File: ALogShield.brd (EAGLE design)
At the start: 53.3 x 77.5 mm, 36 parts, among them IC1 LTC4412, J1 POWER_JACKPTH, Q1 FDN360P, Q2 FDN360P

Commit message: Transitioning to 2.0 update
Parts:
- removed CLOCK_BATT: 3V Backup Battery, SparkFun:BATTCON_12MM_PTH
- removed COUT: 1uF, SmartPrj:C0603-ROUND
- removed C_LDO_SD, C_LDO_SENSE: >=2.2uF, resistor:C0603
- removed DECOUP: >=1uF, resistor:C0603
- removed H0: (no value), SparkFun:SCREWTERMINAL-3.5MM-8
- removed IC1: LTC4412, awickert:TSOT23-6
- removed ISP: AVRISP-6, adafruit:AVRISP
- removed LD0_SD, LD0_SENSE: LP2985, adafruit:SOT23-5L
- removed LED: (no value), SparkFun:LED3MM
- removed LOGO1: OSHW-LOGOM, SparkFun-Aesthetics:OSHW-LOGO-M
- removed LSHIFT: 4050D, 40xx:SO16
- removed MANUAL_LOG: Log Now, awickert:TL_BUTTON
- removed PU1, PU2: 4.7K, rcl:R0603
- removed Q1, Q2: FDN360P, transistor-power:SUPER-SOT3
- removed RSTAT: 470k, rcl:R0603
- removed RTC: DS3231SN, comfile:SO16W
- removed R_LED: 330, rcl:R0603
- removed R_REF_A0: Therm, resistor:0207/10
- removed R_REF_A1, R_REF_A2, R_REF_A3, R_REF_A6, R_REF_A7: (no value), resistor:0207/10
- removed S2: Reset, SparkFun:TACTILE_SWITCH_SMD
- removed U$2: ALOG_LOGO_V1_5.5MM, awickert:ALOG_LOGO_V1_SMALL
- removed U$3: NWLOGO_MED, awickert:NWLOGO_MED
- added 3V3: (no value), csandell:6-TMLF
- added A0, A1, A2, A3: (no value), resistor:0207/10
- added C14: 10nF, rc-master-smd:CECJ-1206
- added CLOCK_BATT1: 3V Backup Battery, SparkFun:BATTCON_12MM_PTH
- added CLOCK_BATT_DECOUP, COUT1: 0.1uF, rcl:C0603
- added CLOCK_BATT_DECOUPLE: 10uF, SparkFun-Passives:EIA3216
- added CLOCK_CIN1, CLOCK_CIN2, CLOCK_CIN3: 1uF, rcl:C0603
- added D1: BAT54C, semicon-smd-ipc:SOT23C
- added D2: BAT54, semicon-smd-ipc:SOT23C
- added H4, H5: (no value), SparkFun-Connectors:SCREWTERMINAL-3.5MM-8
- added ISP1: AVRISP-6, adafruit:AVRISP
- added LED1: (no value), SparkFun:LED3MM
- added LOG: LOG, SparkFun-Electromechanical:TACTILE-PTH
- added LOGO2: OSHW-LOGOM, SparkFun-Aesthetics:OSHW-LOGO-M
- added LSHIFT1: 4050D, 40xx:SO16
- added Q3, Q4: 2N7002PW, SparkFun-DiscreteSemi:SOT323
- added RCKL1, RCLK2: 220, rcl:R0603
- added RESET: Reset, SparkFun-Electromechanical:TACTILE-PTH
- added RN2: 3.3K, resistor-dil:0603-ARC
- added R_LED1: 220, resistor:R0603
- added R_RESET: 10k, rcl:R0603
- added U$1: ALOG_LOGO_V1_5.5MM, awickert:ALOG_LOGO_V1_SMALL
- added U$4: NWLOGO, awickert:NWLOGO
- added U$5: NWLOGO_MED, awickert:NWLOGO_MED
- added U1: DS3231MZ/V+T, Maxim-DS3231MZ_8-SOIC:21-0041B_8
- H2: device SparkFun:SCREWTERMINAL-3.5MM-4 -> SparkFun:SCREWTERMINAL-3.5MM-8
- J1: value POWER_JACKPTH -> (none); device SparkFun:POWER_JACK_PTH -> SparkFun-Connectors:SCREWTERMINAL-3.5MM-4
- moved J1 145.8 mm to (-5.08, -111.1), turned to 0 degrees
- moved H2 113.6 mm to (-4.45, -103.5)
- renumbered SD to SD1
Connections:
- removed net A6: H2.1, R_REF_A6.2
- removed net A7: H2.3, R_REF_A7.2
- removed net BATTERY_POWER: IC1.1, Q1.3
- removed net CD_NOT_CONNECTED: SD1.CD
- removed net D4-SENSE_3V3_SWITCH: LD0_SENSE.3, U$9.D4
- removed net D8-SD_3V3_SWITCH: LD0_SD.3, U$9.D8
- removed net LED+: LED.A, R_LED.2
- removed net N$7: IC1.4, Q2.1, RSTAT.1
- removed net N$8: IC1.5, Q1.1
- removed net VUSB: Q2.3
- new net 5V: H5.9
- new net CS-SD: LSHIFT1.7
- new net D4-SENSE_LDO_SWITCH: 3V3.4, U$9.D4
- new net D6-CLOCK_SD_SWITCH: 3V3.3, U$9.D6
- new net D7-CS-EXT: H5.7, U$9.D7
- new net D8-EXT: H5.6, U$9.D8
- new net DTR: COUT1.1
- new net LED+1: LED1.A, R_LED1.2
- new net N$1: D1.1, RCLK2.1
- new net N$11: D2.3, LOG.3
- new net N$2: CLOCK_BATT1.VCC@1, RCLK2.2
- new net N$67: D1.2, RCKL1.1
- new net SCL_3V3: Q4.2, RN2.3, U1.8
- new net SDA_3V3: Q3.2, RN2.4, U1.7
- net +3V3: now also 3V3.1, CLOCK_CIN2.1, H2.6, H2.8, H5.8; no longer C_LDO_SENSE.2, H0.2, H0.4, H0.6, H0.8, LD0_SENSE.5
- net A0: now also A0.2, C14.C1, H2.1; no longer H0.1, R_REF_A0.2
- net A1: now also A1.2, C14.D1, H2.3; no longer H0.3, R_REF_A1.2
- net A2: now also A2.2, C14.A1, H2.5; no longer H0.5, R_REF_A2.2
- net A3: now also A3.2, C14.B1, H2.7; no longer H0.7, R_REF_A3.2
- net BAT: now also CLOCK_BATT_DECOUP.1, CLOCK_BATT_DECOUPLE.A, D1.3, U1.6; no longer CLOCK_BATT.VCC@1, RTC.14
- net CLK: now also H5.4, ISP1.3, LSHIFT1.3; no longer ISP.3, LSHIFT.3
- net CS: no longer LSHIFT.7
- net D3-INT1: now also H4.3
- net D5_MANUAL_LOG: now also D2.2; no longer MANUAL_LOG.1
- net D6: no longer U$9.D6
- net D7: no longer U$9.D7
- net D9-LED: now also R_LED1.1; no longer R_LED.1
- net DI: now also H5.2, ISP1.4, LSHIFT1.5; no longer ISP.4, LSHIFT.5
- net DO: now also H5.3, ISP1.1; no longer ISP.1
- net GND: now also 3V3.5, A0.1, A1.1, A2.1, A3.1, C14.A2, C14.B2, C14.C2, C14.D2, CLOCK_BATT1.GND, CLOCK_BATT_DECOUP.2, CLOCK_BATT_DECOUPLE.C, CLOCK_CIN1.2, CLOCK_CIN2.2, CLOCK_CIN3.2, H4.6, H5.1, H5.10, ISP1.6, J1.2, LED1.K, LOG.1, LSHIFT1.11, LSHIFT1.14, LSHIFT1.8, LSHIFT1.9, RESET.1, U1.5; no longer CLOCK_BATT.GND, COUT.2, C_LDO_SD.1, C_LDO_SENSE.1, DECOUP.2, IC1.2, IC1.3, ISP.6, J1.GND, J1.GNDBREAK, LD0_SD.2, LD0_SENSE.2, LED.K, LSHIFT.11, LSHIFT.14, LSHIFT.8, LSHIFT.9, MANUAL_LOG.C1, MANUAL_LOG.C2, RTC.10, RTC.11, RTC.12, RTC.13, RTC.5, RTC.6, RTC.7, RTC.8, RTC.9, R_REF_A0.1, R_REF_A1.1, R_REF_A2.1, R_REF_A3.1, R_REF_A6.1, R_REF_A7.1, S2.1, S2.2
- net INT0: now also D2.1, U1.3; no longer MANUAL_LOG.2, RTC.3
- net RESET: now also COUT1.2, ISP1.5, RESET.3, R_RESET.1; no longer ISP.5, S2.3, S2.4
- net RX-I: now also H4.7
- net SCL: now also H4.10, Q4.3, RN2.7; no longer PU1.1, RTC.16
- net SDA: now also H4.9, Q3.3, RN2.8; no longer PU2.1, RTC.15
- net SD_CLK: now also LSHIFT1.2; no longer LSHIFT.2
- net SD_CS: now also LSHIFT1.6; no longer LSHIFT.6
- net SD_DI: now also LSHIFT1.4; no longer LSHIFT.4
- net TX-O: now also H4.8
- net VCC: now also 3V3.6, CLOCK_CIN1.1, H4.5, H5.5, ISP1.2, J1.1, RCKL1.2, RN2.1, RN2.2, R_RESET.2; no longer COUT.1, DECOUP.1, IC1.6, ISP.2, J1.PWR, LD0_SD.1, LD0_SENSE.1, PU1.2, PU2.2, Q1.2, Q2.2, RSTAT.2, RTC.2
- net VDD: now also 3V3.2, CLOCK_CIN3.1, LSHIFT1.1, Q3.1, Q4.1, RN2.5, RN2.6, U1.2; no longer C_LDO_SD.2, LD0_SD.5, LSHIFT.1
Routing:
- net GND: track 329.2 -> 0.00 mm
- net VCC: track 206.1 -> 0.00 mm, vias 2 -> 0
- net +3V3: track 141.0 -> 0.00 mm, vias 1 -> 0
- net RESET: track 99.3 -> 0.00 mm, vias 4 -> 0
- net D4-SENSE_3V3_SWITCH: track 90.7 -> 0.00 mm
- net SCL: track 88.2 -> 0.00 mm, vias 3 -> 0
- net A6: track 86.2 -> 0.00 mm
- net SDA: track 85.9 -> 0.00 mm, vias 3 -> 0
- net A2: track 74.2 -> 0.00 mm
- net VDD: track 66.8 -> 0.00 mm, vias 3 -> 0
- net A1: track 59.4 -> 0.00 mm, vias 1 -> 0
- net DI: track 58.5 -> 0.00 mm, vias 2 -> 0
- net A0: track 57.2 -> 0.00 mm
- net A7: track 54.8 -> 0.00 mm, vias 1 -> 0
- net DO: track 54.0 -> 0.00 mm, vias 1 -> 0
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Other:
- board text added: "25 Jan 2017"
- board text added: "v. 2.0.0 beta"
- board text removed: "27 August 2015"
- board text removed: "3.5-5V"
- board text removed: "3.5-5V!"
- board text removed: "A6"
- board text removed: "A7"
- board text removed: "Unregulated Vin"
- board text removed: "v. 1.0.0, rev. 0"

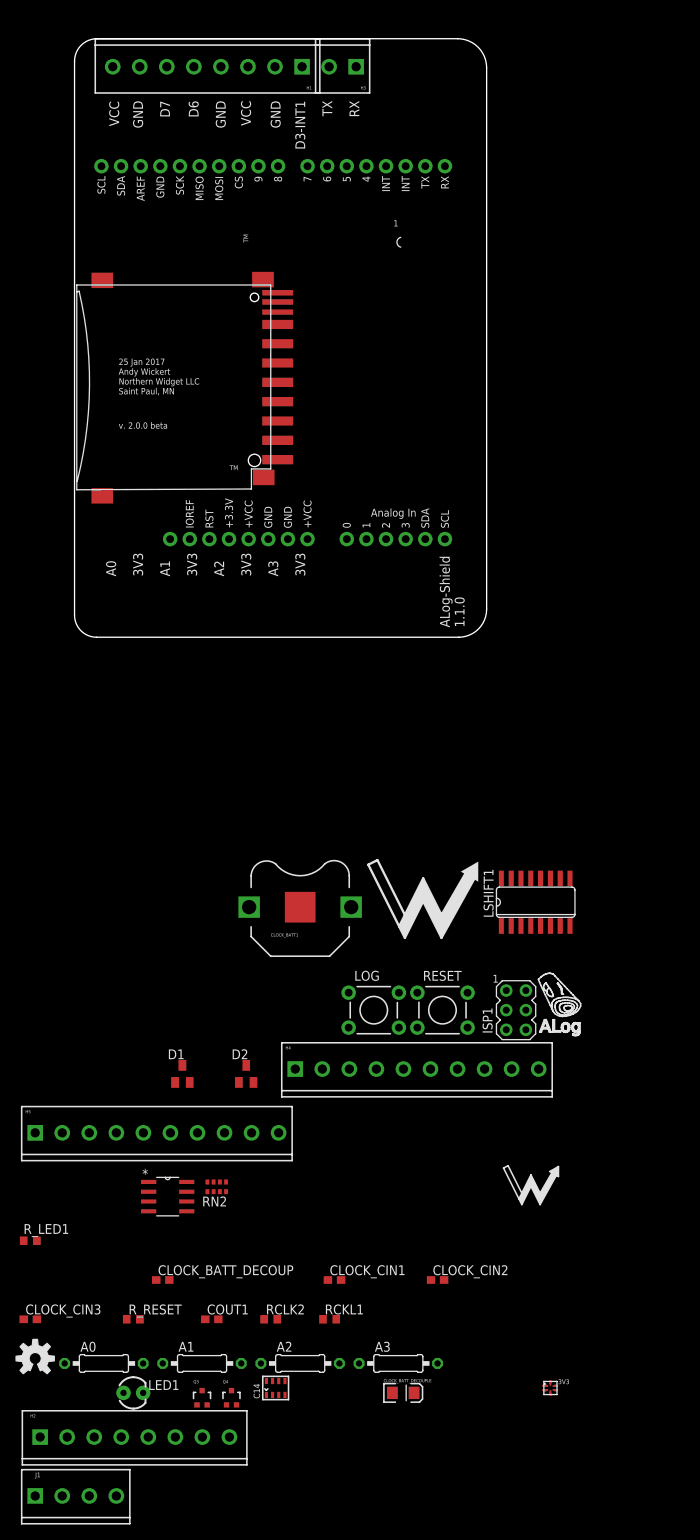
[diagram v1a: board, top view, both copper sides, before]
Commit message: Semi-final parts; not placed or labeled properly
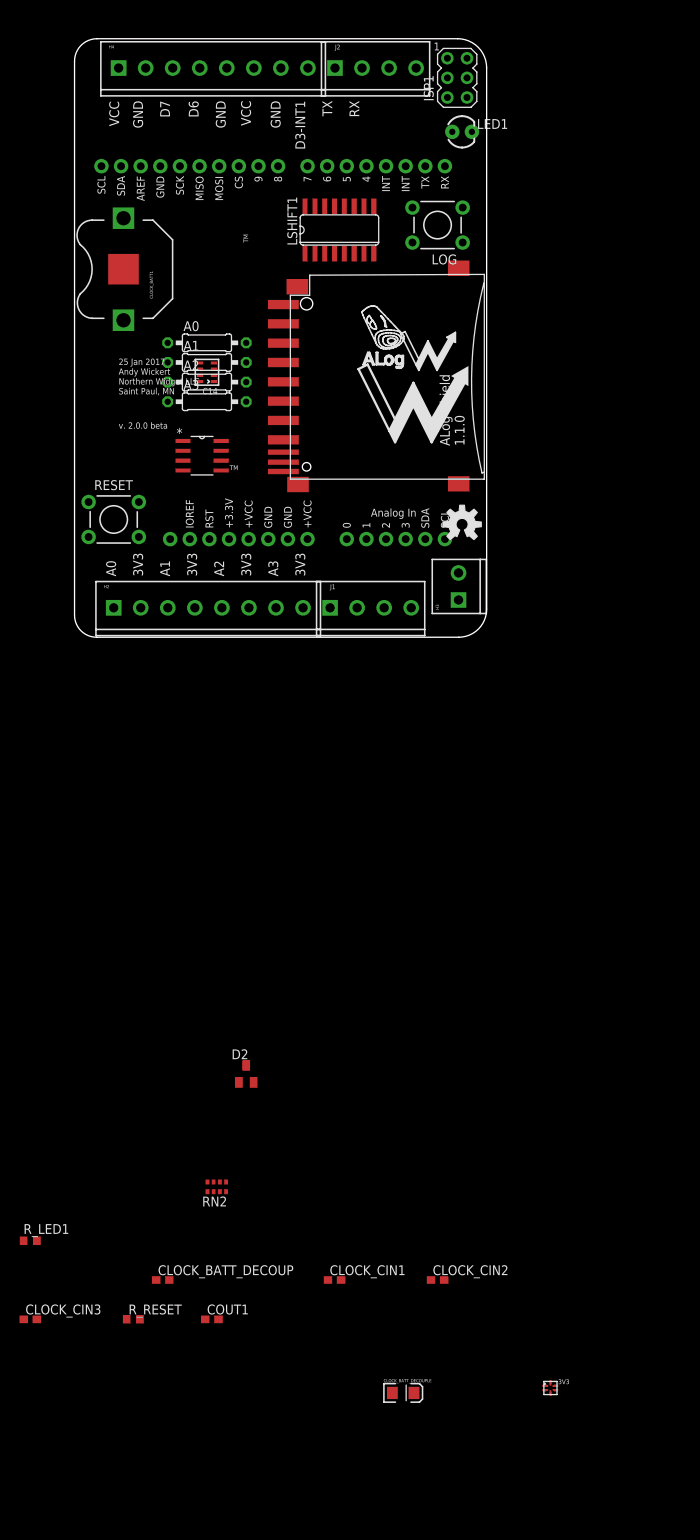
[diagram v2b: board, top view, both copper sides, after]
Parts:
- removed D1: BAT54C, semicon-smd-ipc:SOT23C
- removed H1: (no value), SparkFun:SCREWTERMINAL-3.5MM-8
- removed H5: (no value), SparkFun-Connectors:SCREWTERMINAL-3.5MM-8
- removed Q3, Q4: 2N7002PW, SparkFun-DiscreteSemi:SOT323
- removed RCKL1, RCLK2: 220, rcl:R0603
- added J2: (no value), SparkFun-Connectors:SCREWTERMINAL-3.5MM-4
- H4: device SparkFun-Connectors:SCREWTERMINAL-3.5MM-8 -> SparkFun:SCREWTERMINAL-3.5MM-8
- moved LED1 168.6 mm to (50.2, 65.4)
- moved A0 132.8 mm to (17.1, 38.1)
- moved C14 131.7 mm to (17.1, 34.3), turned to 90 degrees
- moved H4 131.5 mm to (5.71, 73.7)
- moved A1 129.5 mm to (17.1, 35.6)
- moved A2 127.6 mm to (17.1, 33.0)
- moved A3 126.9 mm to (17.1, 30.5)
- moved LOGO2 121.3 mm to (50.2, 14.6)
- moved J1 121.1 mm to (33.1, 3.81)
- moved ISP1 120.9 mm to (49.5, 72.4)
- moved U$5 108.8 mm to (45.7, 37.5)
- moved H2 107.7 mm to (5.08, 3.81)
- moved LOG 101.9 mm to (47.0, 53.3), turned to 180 degrees
- moved U1 96.0 mm to (16.5, 23.5)
- moved LSHIFT1 90.6 mm to (34.3, 52.7)
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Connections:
- removed net 5V: H5.9
- removed net D6: H1.5
- removed net D7: H1.6
- removed net N$1: D1.1, RCLK2.1
- removed net N$2: CLOCK_BATT1.VCC@1, RCLK2.2
- removed net N$67: D1.2, RCKL1.1
- removed net SCL_3V3: Q4.2, RN2.3, U1.8
- removed net SDA_3V3: Q3.2, RN2.4, U1.7
- net +3V3: now also H4.8; no longer H5.8
- net BAT: now also CLOCK_BATT1.VCC@1; no longer D1.3
- net CLK: now also H4.4; no longer H5.4
- net D3-INT1: now also J2.2; no longer H1.1, H4.3
- net D7-CS-EXT: now also H4.7; no longer H5.7
- net D8-EXT: now also H4.6; no longer H5.6
- net DI: now also H4.2; no longer H5.2
- net DO: now also H4.3; no longer H5.3
- net GND: now also H4.1, J2.1; no longer H1.2, H1.4, H1.7, H4.6, H5.1, H5.10
- net RX-I: now also J2.3; no longer H3.1, H4.7
- net SCL: now also J1.4, RN2.3, U1.8; no longer H4.10, Q4.3, RN2.7
- net SDA: now also J1.3, RN2.4, U1.7; no longer H4.9, Q3.3, RN2.8
- net TX-O: now also J2.4; no longer H3.2, H4.8
- net VCC: now also RN2.5, RN2.6, U1.2; no longer H1.3, H1.8, H5.5, RCKL1.2, RN2.1, RN2.2
- net VDD: no longer Q3.1, Q4.1, RN2.5, RN2.6, U1.2
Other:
- board text removed: "1"

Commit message: Update based on new ALog BottleLogger from weeks ago; components not yet placed
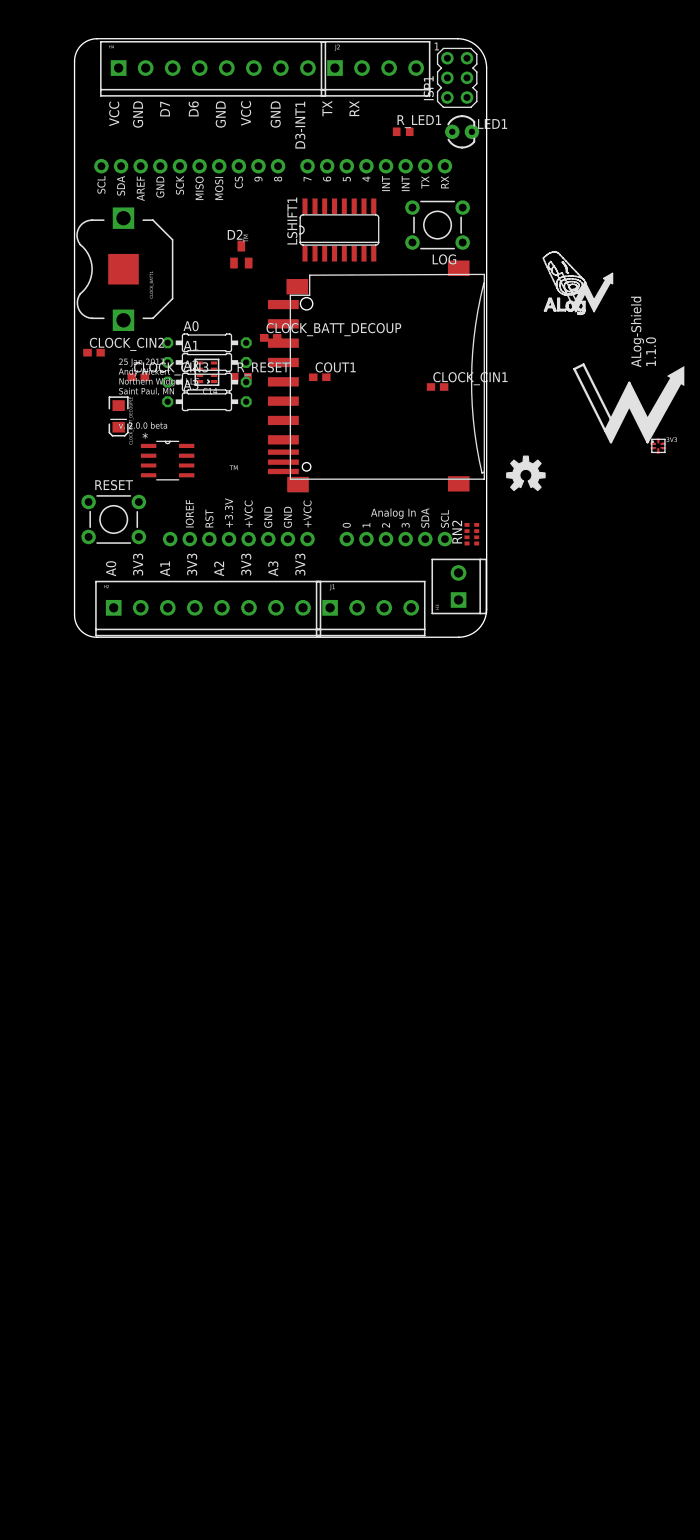
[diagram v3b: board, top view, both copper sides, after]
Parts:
- moved R_LED1 151.4 mm to (42.5, 65.4)
- moved CLOCK_BATT_DECOUPLE 131.6 mm to (5.71, 28.6), turned to 270 degrees
- moved CLOCK_CIN2 128.0 mm to (2.54, 36.8)
- moved 3V3 122.7 mm to (75.6, 24.8)
- moved CLOCK_BATT_DECOUP 122.7 mm to (25.4, 38.7)
- moved CLOCK_CIN3 122.7 mm to (8.26, 33.7)
- moved COUT1 122.7 mm to (31.8, 33.7)
- moved R_RESET 122.7 mm to (21.6, 33.7)
- moved CLOCK_CIN1 116.3 mm to (47.0, 32.4)
- moved D2 106.0 mm to (21.6, 49.5)
- moved RN2 90.7 mm to (51.4, 13.3), turned to 270 degrees
- moved U$4 27.9 mm to (71.8, 29.8)
- moved U$1 24.5 mm to (63.5, 47.0)
- moved U$5 21.7 mm to (66.0, 45.1)
- moved LOGO2 10.4 mm to (58.4, 21.0)
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
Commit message: Components placed
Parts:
- removed RN2: 3.3K, resistor-dil:0603-ARC
- removed U$5: NWLOGO_MED, awickert:NWLOGO_MED
- added SCL_PU, SDA_PU: 10k, rcl:R0603
- moved 3V3 59.1 mm to (18.7, 40.8)
- moved LOGO2 52.7 mm to (5.84, 24.0)
- moved U$1 46.0 mm to (21.3, 28.7)
- moved COUT1 33.4 mm to (42.9, 65.2)
- moved CLOCK_BATT_DECOUPLE 30.8 mm to (21.5, 55.0), turned to 180 degrees
- moved U$4 30.5 mm to (41.3, 30.6)
- moved CLOCK_CIN1 28.6 mm to (20.6, 43.4), turned to 180 degrees
- moved U1 26.5 mm to (16.8, 48.9), turned to 90 degrees
- moved D2 21.7 mm to (42.7, 54.6), turned to 180 degrees
- moved CLOCK_CIN3 14.9 mm to (23.1, 34.8), turned to 90 degrees
- moved CLOCK_BATT_DECOUP 13.5 mm to (22.6, 51.9)
- moved CLOCK_CIN2 12.9 mm to (14.7, 41.1), turned to 180 degrees
- moved R_RESET 12.6 mm to (22.5, 21.1), turned to 90 degrees
- moved C14 11.0 mm to (6.22, 32.8)
- moved A0 10.9 mm to (6.35, 36.6)
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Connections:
- net A0: now also C14.D1; no longer C14.C1
- net A1: now also C14.C1; no longer C14.D1
- net A2: now also C14.B1; no longer C14.A1
- net A3: now also C14.A1; no longer C14.B1
- net CLK: now also H4.2; no longer H4.4
- net DI: now also H4.4; no longer H4.2
- net SCL: now also SCL_PU.1; no longer RN2.3
- net SDA: now also SDA_PU.1; no longer RN2.4
- net VCC: now also SCL_PU.2, SDA_PU.2; no longer RN2.5, RN2.6
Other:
- board size 53.3 x 77.5 mm -> 53.3 x 78.5 mm
- board text added: "ALog-Shield v2.0.0b 25 Jan 2017 Andy Wickert Northern Widget LLC and University of Minnesota"
- board text added: "D8"
- board text added: "MISO"
- board text added: "MOSI"
- board text added: "SCK"
- board text added: "SCL"
- board text added: "SDA"
- board text removed: "25 Jan 2017"
- board text removed: "ALog-Shield 1.1.0"
- board text removed: "Andy Wickert"
- board text removed: "D6"
- board text removed: "Northern Widget LLC"
- board text removed: "Saint Paul, MN"
- board text removed: "v. 2.0.0 beta"

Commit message: Board routed
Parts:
- moved LOGO2 6.60 mm to (12.4, 24.0)
- moved A2 3.94 mm to (10.2, 32.5)
- moved A3 3.94 mm to (10.2, 30.0)
- moved A0 3.94 mm to (10.2, 37.6)
- moved A1 3.94 mm to (10.2, 35.1)
- moved C14 3.94 mm to (10.0, 33.8)
- moved CLOCK_CIN3 3.18 mm to (20.3, 33.3), turned to 0 degrees
- moved 3V3 2.84 mm to (19.9, 38.2)
- moved LSHIFT1 1.61 mm to (34.3, 52.7)
- moved CLOCK_CIN1 1.30 mm to (21.8, 43.7)
- moved CLOCK_CIN2 1.14 mm to (13.7, 41.7)
- moved D2 1.02 mm to (42.7, 53.6)
- moved SD1 0.51 mm to (27.9, 34.2)
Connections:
- removed net CS: U$9.D10
- net CS-SD: now also U$9.D10
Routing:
- net VCC: track 0.00 -> 191.0 mm
- net +3V3: track 0.00 -> 143.9 mm, vias 0 -> 1
- net DO: track 0.00 -> 127.1 mm
- net RESET: track 0.00 -> 120.5 mm
- net SCL: track 0.00 -> 103.8 mm
- net CLK: track 0.00 -> 99.0 mm
- net SDA: track 0.00 -> 99.0 mm
- net DI: track 0.00 -> 76.1 mm, vias 0 -> 1
- net A0: track 0.00 -> 71.5 mm
- net A1: track 0.00 -> 68.0 mm
- net A2: track 0.00 -> 64.4 mm
- net A3: track 0.00 -> 62.1 mm
- net VDD: track 0.00 -> 50.5 mm
- net INT0: track 0.00 -> 45.8 mm
- net D9-LED: track 0.00 -> 41.3 mm
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- added copper zone on layer 1, net GND
- added copper zone on layer 16, net GND
